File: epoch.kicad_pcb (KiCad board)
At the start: 2 copper layers, 30 x 30 mm, 35 parts, among them J1 USB_OTG, J2 CONN_01X05, P3 CONN_01X10, Q1 DMP1045U, SW1 SW_Reset, SW2 SW_Up, SW3 SW_Middle, SW4 SW_Down, U1 MIC5219-3.3BM5, U2 ATSAMD21Ennc-AU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

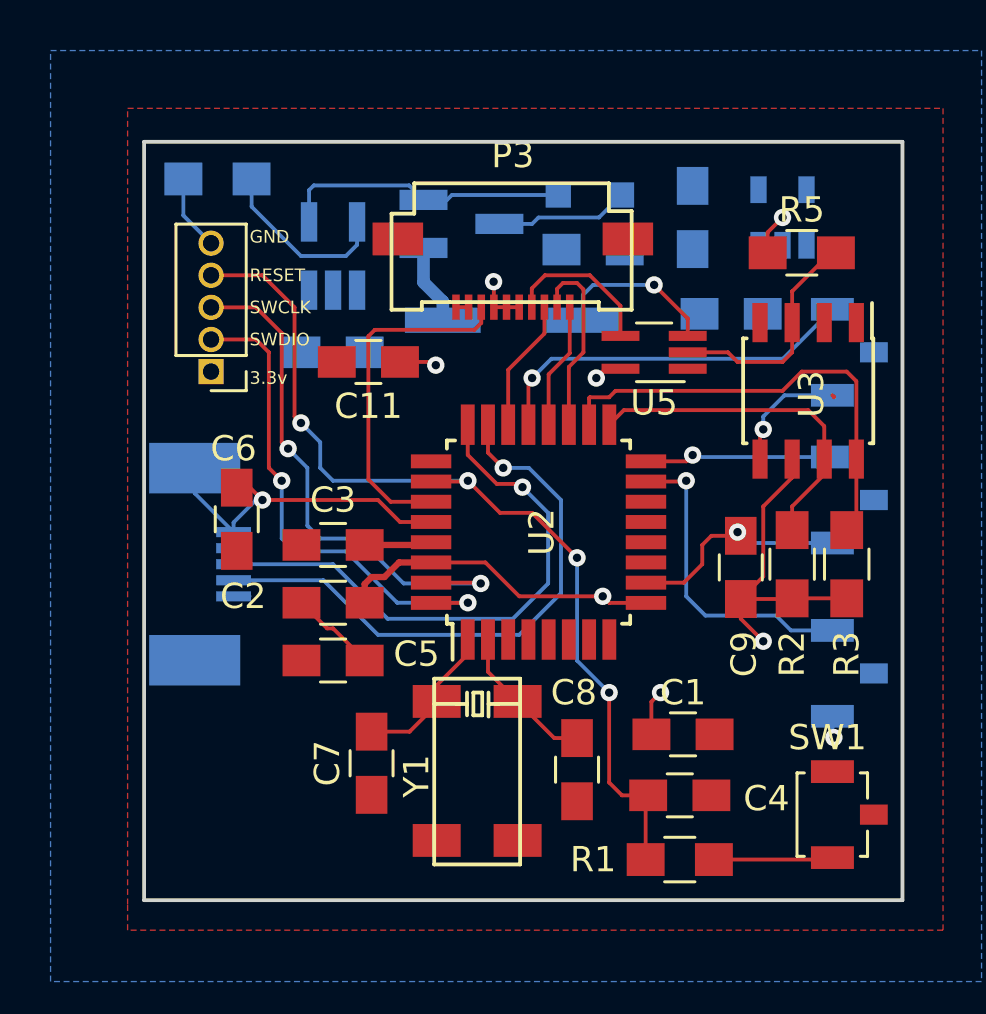
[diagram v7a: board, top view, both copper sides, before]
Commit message: More connections
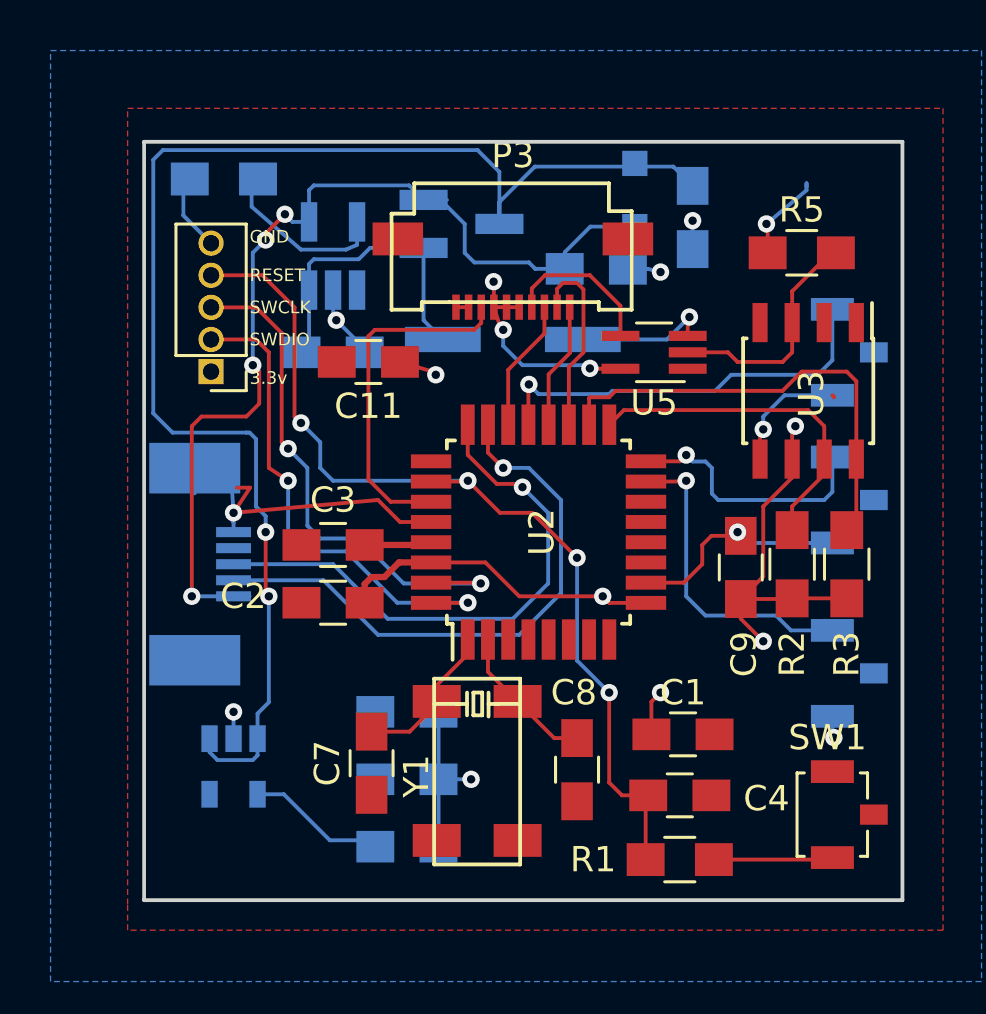
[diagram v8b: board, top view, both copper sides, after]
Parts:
- C5, C6: moved to B.Cu
- moved U1 30.7 mm to (151.5, 124.7), turned to 270 degrees
- moved C14 22.4 mm to (158.4, 125.2)
- moved C6 10.2 mm to (158.4, 122.6), turned to 0 degrees
- moved C5 7.92 mm to (158.4, 127.9)
- moved D1 1.78 mm to (167.4, 102.1), turned to 270 degrees
- moved C10 0.77 mm to (165.9, 105.0)
- moved BT1 0.76 mm to (162.6, 107.8)
- moved R4 0.25 mm to (151.2, 101.5)
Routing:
- net (+5): track 5.30 -> 56.8 mm, vias 0 -> 2
- net Net-(C10-Pad1): track 12.7 -> 39.9 mm, vias 0 -> 4
- net (GND): track 41.8 -> 52.0 mm, vias 5 -> 10
- net (+3.3): track 34.3 -> 43.9 mm, vias 7 -> 9
- net Net-(BT1-Pad1): track 3.66 -> 12.3 mm
- net Net-(C5-Pad2): track 0.11 -> 5.52 mm
- net BUT_MID: track 7.51 -> 10.3 mm
- net BUT_DWN: track 14.9 -> 16.3 mm
